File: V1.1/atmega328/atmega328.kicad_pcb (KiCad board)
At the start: 2 copper layers, 71.9 x 27 mm, 39 parts, among them SW1 SW_Push, SW2 SW_Push, SW3 SW_SPDT, U1 ATmega328P-AU, U2 TPS62203DBV, U3 LM386, Y1 Crystal

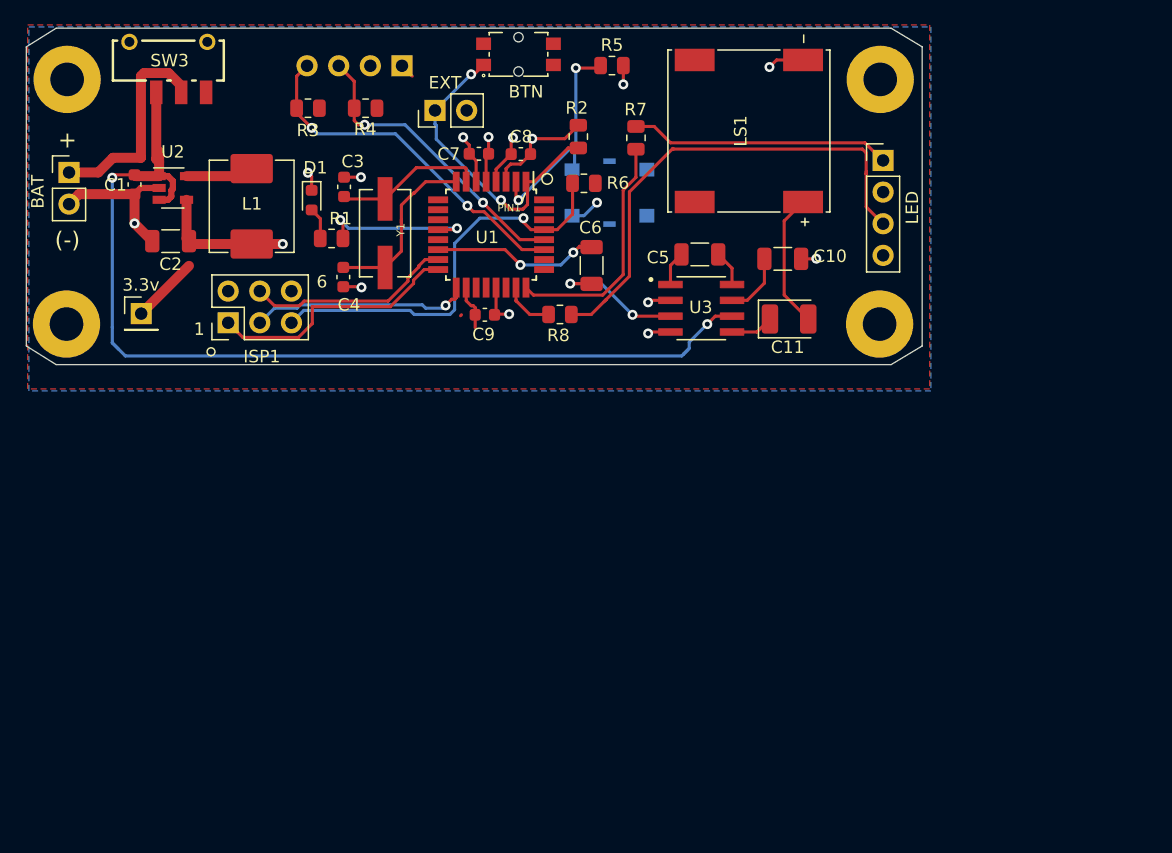
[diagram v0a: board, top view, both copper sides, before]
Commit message: recreating lost AS5048 version
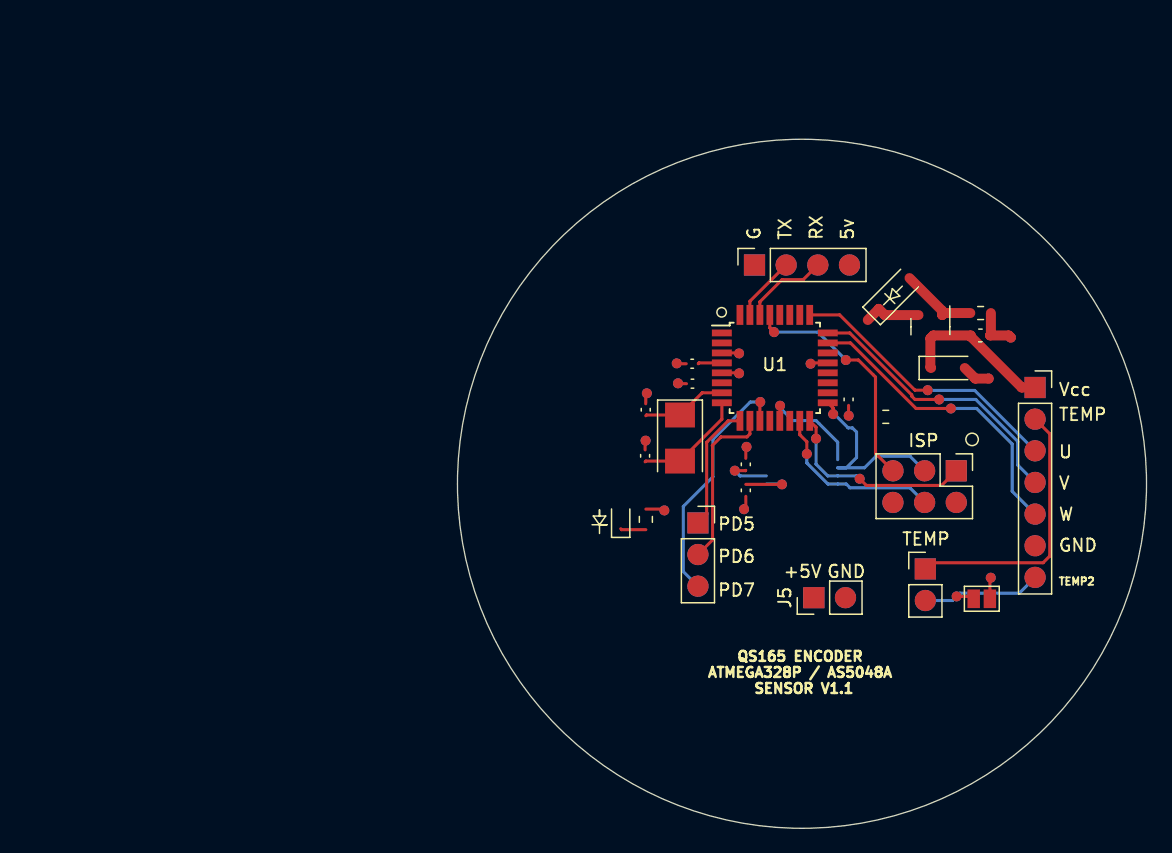
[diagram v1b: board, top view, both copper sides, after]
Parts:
- removed 3.3v1: Conn_01x01, Connector_PinHeader_2.54mm:PinHeader_1x01_P2.54mm_Vertical
- removed BAT1, SWTCH1: Conn_01x02, Connector_PinHeader_2.54mm:PinHeader_1x02_P2.54mm_Vertical
- removed C1: 4.7u1, Capacitor_SMD:C_0603_1608Metric
- removed C10: 1uF, Capacitor_SMD:C_1206_3216Metric
- removed C11: 220uF, Capacitor_Tantalum_SMD:CP_EIA-3528-12_Kemet-T
- removed C2: 10u1, Capacitor_SMD:C_1206_3216Metric
- removed C3: 22p1, Capacitor_SMD:C_0603_1608Metric
- removed C4: 22p2, Capacitor_SMD:C_0603_1608Metric
- removed C5, C6: 10uF, Capacitor_SMD:C_1206_3216Metric
- removed C7, C8, C9: 0.1uF, Capacitor_SMD:C_0603_1608Metric
- removed D1: LED, LED_SMD:LED_0603_1608Metric
- removed ISP1: Conn_02x03_Top_Bottom, Connector_PinSocket_2.54mm:isp_6pin
- removed L1: L, Inductor_SMD:L_Abracon_ASPI-0630LR
- removed LED1, OLED1: Conn_01x04, Connector_PinHeader_2.54mm:PinHeader_1x04_P2.54mm_Vertical
- removed LS1: Speaker, CDS-13138-SMT-TR:SPKR_CDS-13138-SMT-TR
- removed R1: 220, Resistor_SMD:R_0805_2012Metric
- removed R2, R3, R4, R5, R6: 10k, Resistor_SMD:R_0805_2012Metric
- removed R7, R8: 330, Resistor_SMD:R_0805_2012Metric
- removed REF** (x4): MountingHole_2.7mm_Pad, MountingHole:MountingHole_2.7mm_Pad
- removed SW1: SW_Push, wurth_momentary:436331045822
- removed SW2: SW_Push, 431181015816:431181015816
- removed SW3: SW_SPDT, wurth_slide_switch:450405020524
- removed U1: ATmega328P-AU, Package_QFP:TQFP-32_7x7mm_P0.8mm
- removed U2: TPS62203DBV, Package_TO_SOT_SMD:SOT-23-5
- removed U3: LM386, LM386MX-1_NOPB:SOIC127P599X175-8N
- removed Y1: Crystal, ECS-120-20-3X-EN-TR:XTAL_ECS-120-20-3X-EN-TR
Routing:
- net (no net): track 0.00 -> 302.7 mm
- net VCC: track 81.4 -> 0.00 mm, vias 2 -> 0
- net GND: track 42.5 -> 0.00 mm, vias 12 -> 0
- net Net-(LED1-Pad3): track 40.0 -> 0.00 mm
- net RESET: track 33.0 -> 0.00 mm, vias 1 -> 0
- net 3.3V: track 32.1 -> 0.00 mm, vias 4 -> 0
- net SDA: track 28.5 -> 0.00 mm, vias 2 -> 0
- net BTN1: track 24.8 -> 0.00 mm, vias 2 -> 0
- net SCL: track 24.1 -> 0.00 mm, vias 2 -> 0
- net Net-(LED1-Pad1): track 21.0 -> 0.00 mm
- net MISO: track 20.5 -> 0.00 mm
- net LED2: track 19.2 -> 0.00 mm
- net BTN2: track 18.3 -> 0.00 mm, vias 2 -> 0
- net SCK: track 17.6 -> 0.00 mm, vias 1 -> 0
- net Net-(BAT1-Pad1): track 17.3 -> 0.00 mm
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- removed copper zone on F.Cu, net 3.3V
- removed copper zone on B.Cu, net GND
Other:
- board size 71.9 x 27 mm -> 55.3 x 55.3 mm
- net class Default removed
- board text removed: "(-)"
- board text removed: "+"
- board text removed: "1"
- board text removed: "2"
- board text removed: "3.3v"
- board text removed: "5"
- board text removed: "6"
- board text removed: "ADJUST"
- board text removed: "BAT"
- board text removed: "BAT+"
- board text removed: "BTN"
- board text removed: "EXT"
- board text removed: "GND"
- board text removed: "ISP"
- board text removed: "LED"
- board text removed: "LED1"
- board text removed: "LED2"
- board text removed: "PIN1"
- board text removed: "PWR"
- board text removed: "SDA"
- board text removed: "TRIGGER"
- board text removed: "raygun_v1.0"

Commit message: recreating lost AS5048 version
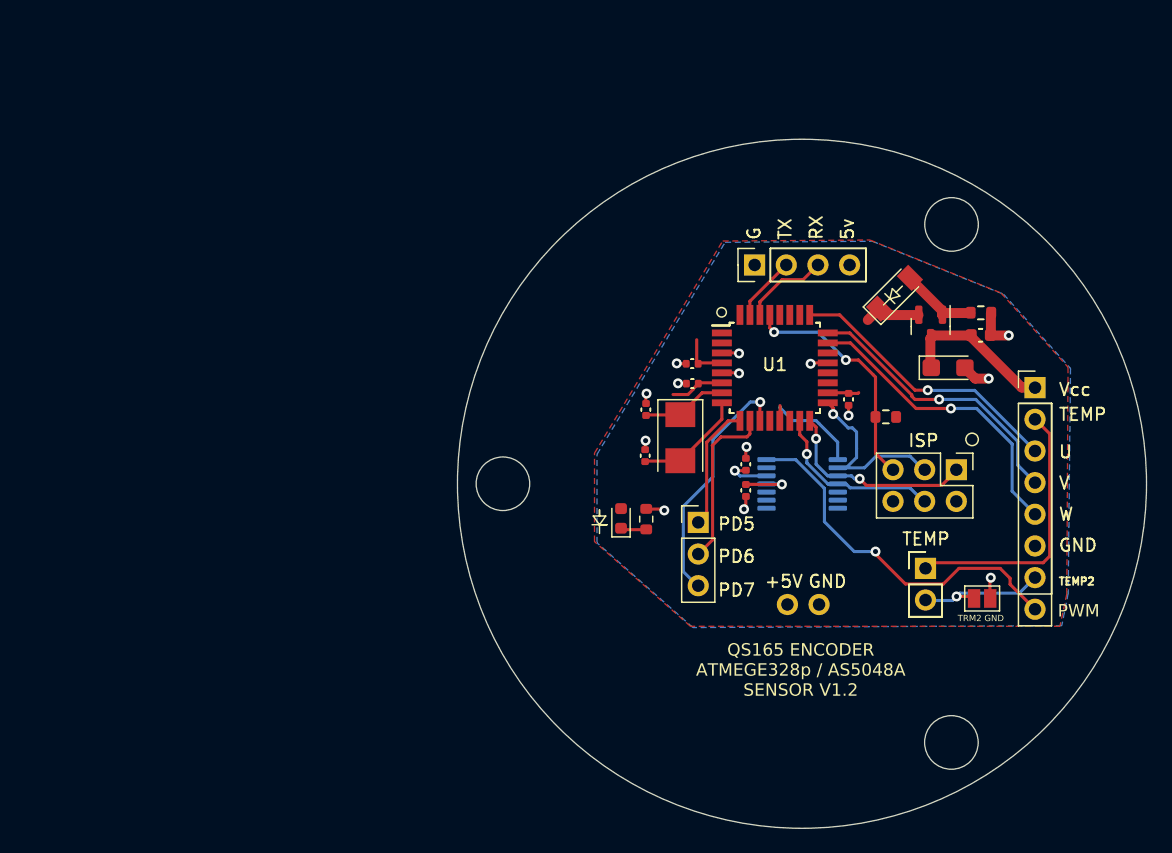
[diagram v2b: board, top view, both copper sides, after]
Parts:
- added ?: , , F.Cu at (156.8, 125.3)
- added C1: 100n, Capacitor_SMD:C_0603_1608Metric, F.Cu at (159.2, 92.6)
- added C2: 4.7, Capacitor_Tantalum_SMD:CP_EIA-3216-18_Kemet-A, F.Cu at (156.6, 95.2)
- added C3: 100n, Capacitor_SMD:C_0402_1005Metric, F.Cu at (148.6, 97.8)
- added C4: 100n, Capacitor_SMD:C_0402_1005Metric, F.Cu at (136.0, 94.9)
- added C5: 100n, Capacitor_SMD:C_0402_1005Metric, F.Cu at (136.1, 96.5)
- added C6: 20p, Capacitor_SMD:C_0402_1005Metric, F.Cu at (132.3, 98.6)
- added C7: 20p, Capacitor_SMD:C_0402_1005Metric, F.Cu at (132.3, 102.3)
- added C8: 100n, Capacitor_SMD:C_0402_1005Metric, F.Cu at (140.3, 105.1)
- added C9: 10, Capacitor_SMD:C_0402_1005Metric, F.Cu at (140.3, 103.0)
- added D1: BZV55C6V2, Diode_SMD:D_MiniMELF, F.Cu at (152.3, 89.3)
- added D2: RED_LED, LED_SMD:LED_0603_1608Metric, F.Cu at (130.3, 107.3)
- added G***: LOGO, 431181015816:monkey, B.Cu at (145.0, 116.2)
- added ISP1: Conn_02x03_Top_Bottom, Connector_PinSocket_2.54mm:isp_6pin, F.Cu at (157.2, 106.0)
- added J1: Conn_01x04, Connector_PinHeader_2.54mm:PinHeader_1x04_P2.54mm_Vertical, F.Cu at (141.1, 87.0)
- added J2: Conn_01x02, Connector_PinHeader_2.54mm:myPinHeader_1x02_P2.54mm_Vertical, F.Cu at (143.7, 114.2)
- added J3: Conn_01x02_Male, Connector_PinHeader_2.54mm:PinHeader_1x02_P2.54mm_Vertical, F.Cu at (154.8, 111.3)
- added J4: Conn_01x03, Connector_PinHeader_2.54mm:PinHeader_1x03_P2.54mm_Vertical, F.Cu at (136.5, 107.7)
- added J5: Conn_01x08, Connector_PinHeader_2.54mm:PinHeader_1x08_P2.54mm_Vertical, F.Cu at (163.6, 96.8)
- added JP1: SolderJumper_2_Open, Jumper:SolderJumper-2_P1.3mm_Open_Pad1.0x1.5mm, F.Cu at (159.3, 113.8)
- added Q1: Si2319CDS, Package_TO_SOT_SMD:SOT-23, F.Cu at (155.2, 91.9)
- added R1: 100k, Resistor_SMD:R_0603_1608Metric, F.Cu at (159.2, 90.8)
- added R2: 10k, Resistor_SMD:R_0603_1608Metric, F.Cu at (151.6, 99.2)
- added R3: 20k, Resistor_SMD:R_0603_1608Metric, F.Cu at (132.3, 107.4)
- added REF**: MountingHole_4.3mm_M4, MountingHole:MountingHole_4.3mm_M4, F.Cu at (156.8, 83.8)
- added REF**: MountingHole_4.3mm_M4, MountingHole:MountingHole_4.3mm_M4, F.Cu at (120.8, 104.6)
- added U1: ATmega328P-AU, Package_QFP:TQFP-32_7x7mm_P0.8mm, F.Cu at (142.7, 95.3)
- added U2: AS5048A, Package_SO:TSSOP-14_4.4x5mm_P0.65mm, B.Cu at (144.9, 104.6)
- added Y1: Crystal, Crystal:Crystal_SMD_5032-2Pin_5.0x3.2mm, F.Cu at (135.1, 100.9)
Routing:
- net (no net): track 302.7 -> 0.00 mm
- net PWM: track 0.00 -> 29.5 mm, vias 0 -> 1
- net W: track 0.00 -> 24.5 mm, vias 0 -> 1
- net V: track 0.00 -> 22.8 mm, vias 0 -> 1
- net U: track 0.00 -> 22.6 mm, vias 0 -> 1
- net TRM1: track 0.00 -> 21.9 mm
- net PD7: track 0.00 -> 19.8 mm, vias 0 -> 1
- net +5V: track 0.00 -> 19.6 mm, vias 0 -> 1
- net RESET: track 0.00 -> 19.3 mm, vias 0 -> 2
- net GND: track 0.00 -> 19.0 mm, vias 0 -> 14
- net MISO: track 0.00 -> 16.1 mm, vias 0 -> 2
- net SCK: track 0.00 -> 15.3 mm, vias 0 -> 1
- net MOSI: track 0.00 -> 14.4 mm, vias 0 -> 1
- net PD6: track 0.00 -> 13.7 mm
- net Vcc: track 0.00 -> 12.7 mm
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- added copper zone on F.Cu, net +5V
- added copper zone on B.Cu, net GND
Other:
- board text added: "PWM"
- board text added: "QS165 ENCODER ATMEGE328p / AS5048A SENSOR V1.2"
- board text added: "TRM2 GND"
- board text added: "lyotmonky"
